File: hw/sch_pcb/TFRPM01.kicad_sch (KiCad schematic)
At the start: 28 parts, among them J1 HEADER_1x03_Horizontal, J2 SM04B-GHS-TB, J3 SM04B-GHS-TB, M2 M3, U1 PCF8583T, U2 SN74LVC1G14QDCKRQ1, U3 MIC5504-3.3YM5

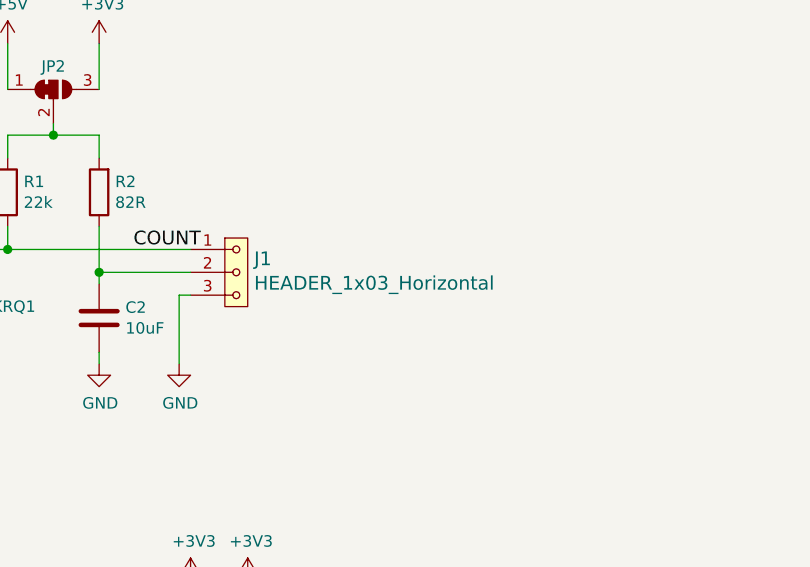
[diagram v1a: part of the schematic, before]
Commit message: Change type marking of pin_header.
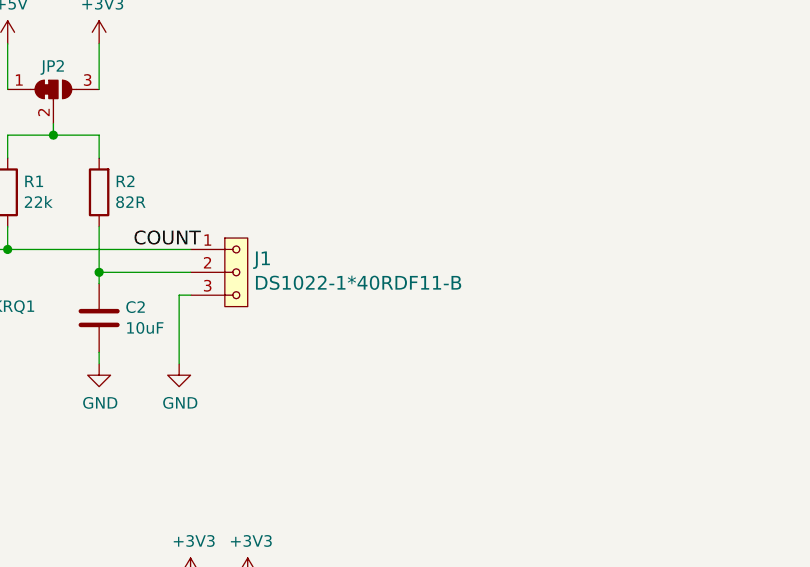
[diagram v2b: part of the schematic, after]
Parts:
- J1: value HEADER_1x03_Horizontal -> DS1022-1*40RDF11-B
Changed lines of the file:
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@@
     (pin "2")
     (pin "4")
-    (pin "3")
-    (pin "5")
   )
   (symbol (lib_name "LED_1") (lib_id "Device:LED") (at 104.14 63.5 0) (unit 1)
@@
       (effects (font (size 1.524 1.524)) (justify left))
     )
-    (property "Value" "HEADER_1x03_Horizontal" (id 1) (at 165.8112 67.2592 0)
+    (property "Value" "DS1022-1*40RDF11-B" (id 1) (at 165.8112 67.2592 0)
       (effects (font (size 1.524 1.524)) (justify left))
     )
@@
       (effects (font (size 1.524 1.524)) hide)
     )
-    (property "Datasheet" "" (id 3) (at 163.83 63.5 0)
-      (effects (font (size 1.524 1.524)))
+    (property "Datasheet" "5c70984412875079b91f879d" (id 3) (at 163.83 63.5 0)
+      (effects (font (size 1.524 1.524)) hide)
     )
     (pin "1")
@@
       (effects (font (size 1.27 1.27)) hide)
     )
-    (pin "2")
-    (pin "4")
     (pin "3")
     (pin "5")
@@
     )
     (path "/00000000-0000-0000-0000-00005de84efb"
-      (reference "J1") (unit 1) (value "HEADER_1x03_Horizontal") (footprint "Connector_PinHeader_2.54mm:PinHeader_1x03_P2.54mm_Horizontal")
+      (reference "J1") (unit 1) (value "DS1022-1*40RDF11-B") (footprint "Connector_PinHeader_2.54mm:PinHeader_1x03_P2.54mm_Horizontal")
     )
     (path "/00000000-0000-0000-0000-00005deb9c07"

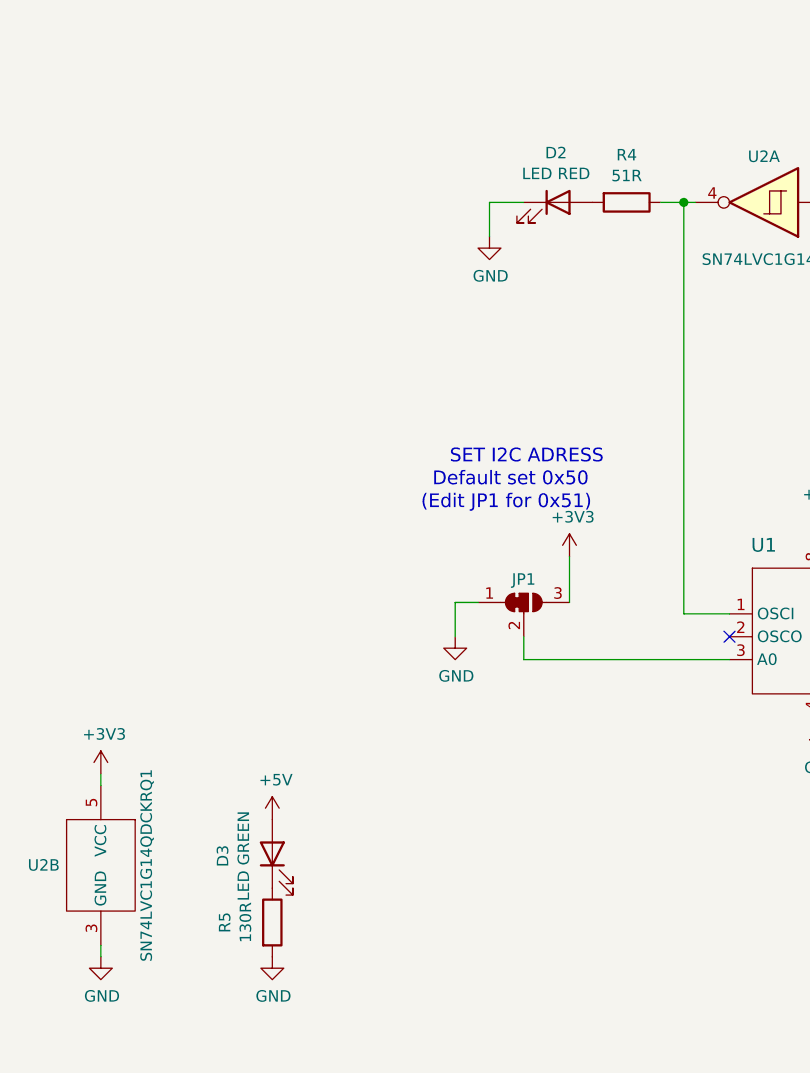
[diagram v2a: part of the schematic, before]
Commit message: Update LEDs part numbers.
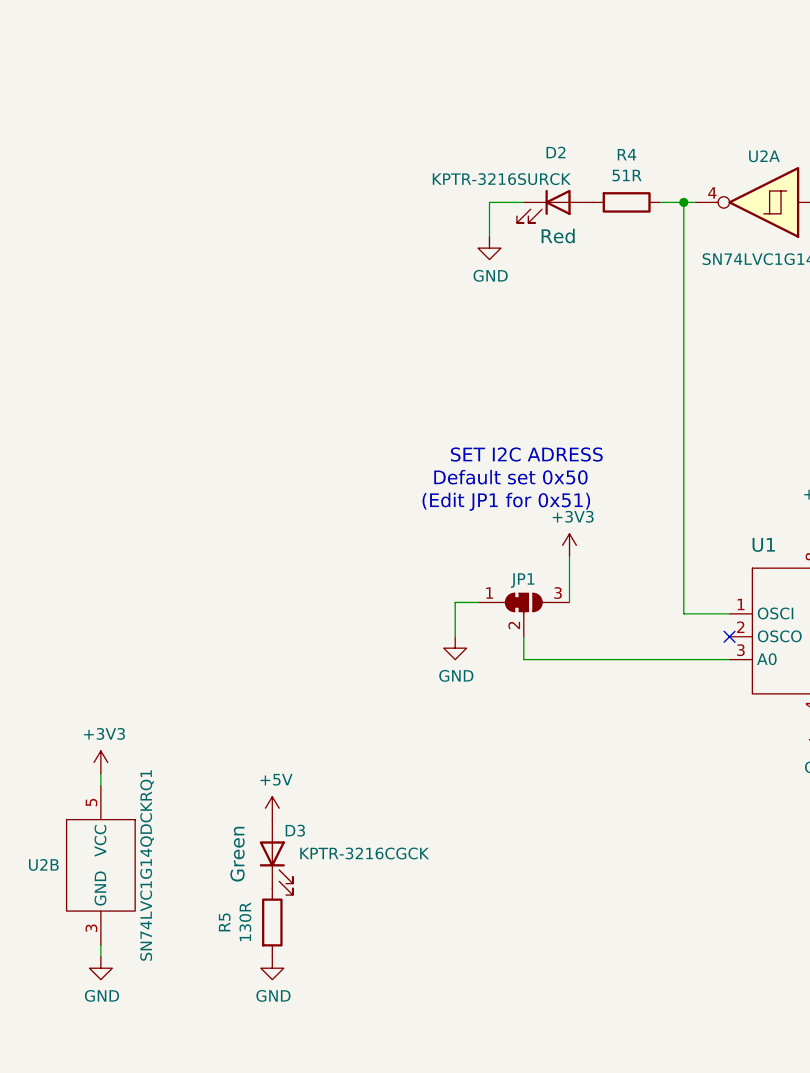
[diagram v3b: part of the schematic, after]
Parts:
- D2: value LED RED -> KPTR-3216SURCK; Color (none) -> Red; UST_ID 5c70984412875079b91f8896 -> (none)
- D3: value LED GREEN -> KPTR-3216CGCK; Color (none) -> Green; UST_ID 5c70984412875079b91f8895 -> (none)
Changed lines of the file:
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@@
     (pin "2")
     (pin "4")
+    (pin "3")
+    (pin "5")
   )
   (symbol (lib_name "LED_1") (lib_id "Device:LED") (at 104.14 63.5 0) (unit 1)
     (in_bom yes) (on_board yes)
     (property "Reference" "D2" (id 0) (at 103.9114 58.0136 0))
-    (property "Value" "LED RED" (id 1) (at 103.9114 60.325 0))
+    (property "Value" "KPTR-3216SURCK" (id 1) (at 97.79 60.96 0))
     (property "Footprint" "Mlab_D:LED_1206_2" (id 2) (at 104.14 63.5 0)
       (effects (font (size 1.27 1.27)) hide)
     )
-    (property "Datasheet" "~" (id 3) (at 104.14 63.5 0)
-      (effects (font (size 1.27 1.27)) hide)
-    )
-    (property "UST_ID" "5c70984412875079b91f8896" (id 5) (at 104.14 63.5 0)
-      (effects (font (size 1.27 1.27)) hide)
+    (property "Datasheet" "https://www.tme.eu/Document/abfabb2e369b55022af776cff528b52b/kptr-3216surck.pdf" (id 3) (at 104.14 63.5 0)
+      (effects (font (size 1.27 1.27)) hide)
+    )
+    (property "Color" "Red" (id 5) (at 104.14 67.31 0)
+      (effects (font (size 1.524 1.524)))
     )
     (pin "1")
@@
       (effects (font (size 1.27 1.27)) hide)
     )
+    (pin "2")
+    (pin "4")
     (pin "3")
     (pin "5")
@@
   (symbol (lib_id "Device:LED") (at 72.39 135.89 90) (unit 1)
     (in_bom yes) (on_board yes)
-    (property "Reference" "D3" (id 0) (at 66.9036 136.1186 0))
-    (property "Value" "LED GREEN" (id 1) (at 69.215 136.1186 0))
+    (property "Reference" "D3" (id 0) (at 74.93 133.35 90))
+    (property "Value" "KPTR-3216CGCK" (id 1) (at 82.55 135.89 90))
     (property "Footprint" "Mlab_D:LED_1206_2" (id 2) (at 72.39 135.89 0)
       (effects (font (size 1.27 1.27)) hide)
     )
-    (property "Datasheet" "~" (id 3) (at 72.39 135.89 0)
-      (effects (font (size 1.27 1.27)) hide)
-    )
-    (property "UST_id" "" (id 4) (at 72.39 135.89 0)
-      (effects (font (size 1.27 1.27)) hide)
-    )
-    (property "UST_ID" "5c70984412875079b91f8895" (id 5) (at 72.39 135.89 0)
-      (effects (font (size 1.27 1.27)) hide)
+    (property "Datasheet" "https://www.tme.eu/Document/283cf8402cc8d70fa16840405395cb5a/kptr-3216cgck.pdf" (id 3) (at 72.39 135.89 0)
+      (effects (font (size 1.27 1.27)) hide)
+    )
+    (property "Color" "Green" (id 5) (at 68.58 135.89 0)
+      (effects (font (size 1.524 1.524)))
     )
     (pin "1")
@@
     )
     (path "/00000000-0000-0000-0000-00005b1bc617"
-      (reference "D2") (unit 1) (value "LED RED") (footprint "Mlab_D:LED_1206_2")
+      (reference "D2") (unit 1) (value "KPTR-3216SURCK") (footprint "Mlab_D:LED_1206_2")
     )
     (path "/158af5df-cc1b-4506-bbe6-cb7505295b5b"
-      (reference "D3") (unit 1) (value "LED GREEN") (footprint "Mlab_D:LED_1206_2")
+      (reference "D3") (unit 1) (value "KPTR-3216CGCK") (footprint "Mlab_D:LED_1206_2")
     )
     (path "/457f929f-17ed-4eee-8eba-3af909e8c516"
